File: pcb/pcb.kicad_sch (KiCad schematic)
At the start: 4 parts, among them U1 STM32G070RBTx

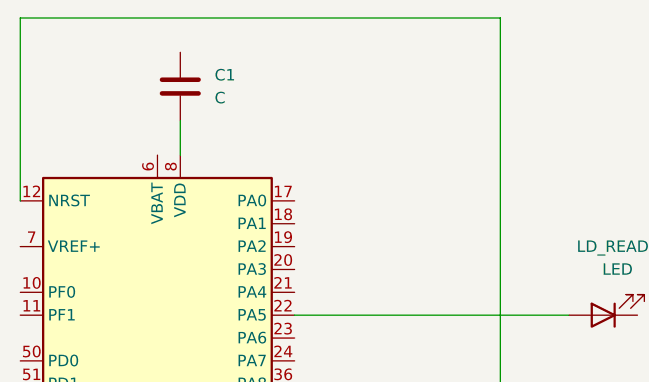
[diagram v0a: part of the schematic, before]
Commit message: kicad: add C1 value
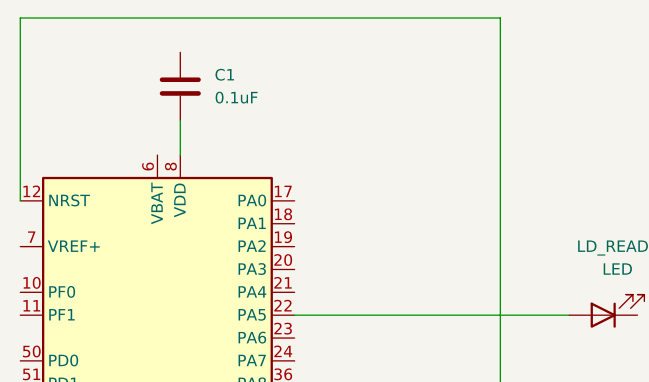
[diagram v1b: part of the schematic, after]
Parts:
- C1: value C -> 0.1uF
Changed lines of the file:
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@@
 			)
 		)
-		(property "Value" "C"
+		(property "Value" "0.1uF"
 			(at 146.05 39.3699 0)
 			(effects

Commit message: kicad: add usb-c symbol and 5V source
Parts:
- added J2: 12402012E212A, 12402012E212A_AMP, symbol 12402012E212A:12402012E212A
- renumbered DEBUG to J1
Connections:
- net VCC is gone; now on net +3.3V: J1.1 (Pin_1)
- net +3.3V: now reaches C1.1
- new net +5V: J2.A1-B12 (GND), J2.B4-A9 (VBUS)
